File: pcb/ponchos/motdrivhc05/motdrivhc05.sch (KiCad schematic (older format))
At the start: 21 parts, among them J1 Screw_Terminal_1x06, J3 GW-040, J4 CONN_01X02, Q1 TIP31, U1 L293

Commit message: Agregado y modificado de nombres de nets en esquemático. Agregado de serigrafías con referencias en PCB.
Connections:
- net M1A: now also D1.2 (A), D5.1 (K), J1.4, U1.3 (1Y); no longer SH1.8, U1.2 (1A)
- net M2A: now also D3.2 (A), D7.1 (K), J1.6, U1.11 (3Y); no longer SH1.11 ((*/MOSI)_11), U1.7 (2A)
- net M2B: now reaches D4.2 (A), D8.1 (K), J1.5, U1.14 (4Y)
- net M1B: now reaches D2.2 (A), D6.1 (K), J1.3, U1.6 (2Y)
- net EXT: now reaches D9.1 (K), J4.2 (P2), Q1.2 (C)
- net M3A renamed 3A
- net M4A renamed 4A
- new net 1A: SH1.8, U1.2 (1A)
- new net 2A: SH1.11 ((*/MOSI)_11), U1.7 (2A)
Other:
- moved on the sheet: D9, J4
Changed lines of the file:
@@
 Connection ~ 6600 3675
 Wire Wire Line
-	7225 2375 10000 2375
-Wire Wire Line
-	7150 2575 9875 2575
-Wire Wire Line
-	7150 2775 9975 2775
-Wire Wire Line
-	7225 2975 9875 2975
+	7225 2375 9325 2375
+Wire Wire Line
+	7150 2575 9200 2575
+Wire Wire Line
+	7150 2775 9325 2775
+Wire Wire Line
+	7225 2975 9225 2975
 Wire Wire Line
 	7750 3350 7750 3450
@@
 	6400 1050 6400 1800
 Text Label 5775 2200 2    60   ~ 0
-M1A
+1A
 Wire Wire Line
 	6000 2200 5775 2200
 Text Label 5775 2400 2    60   ~ 0
-M2A
+2A
 Wire Wire Line
 	6000 2400 5775 2400
@@
 	6000 2800 5775 2800
 Text Label 5775 3000 2    60   ~ 0
-M3A
+3A
 Wire Wire Line
 	6000 3000 5775 3000
 Text Label 5775 3200 2    60   ~ 0
-M4A
+4A
 Wire Wire Line
 	6000 3200 5775 3200
 Text Label 3800 3450 0    60   ~ 0
-M1A
+1A
 Wire Wire Line
 	3575 3450 3800 3450
 Text Label 3800 3075 0    60   ~ 0
-M2A
+2A
 Wire Wire Line
 	3575 3075 3800 3075
@@
 	3575 3200 3800 3200
 Text Label 3800 2950 0    60   ~ 0
-M3A
+3A
 Wire Wire Line
 	3575 2950 3800 2950
 Text Label 3800 2825 0    60   ~ 0
-M4A
+4A
 Wire Wire Line
 	3575 2825 3800 2825
@@
 L CONN_01X02 J4
 U 1 1 59A1C921
-P 4900 5725
-F 0 "J4" H 4900 5875 50  0000 C CNN
-F 1 "CONN_01X02" V 5000 5725 50  0000 C CNN
-F 2 "Pin_Headers:Pin_Header_Straight_1x02" H 4900 5725 50  0001 C CNN
-F 3 "" H 4900 5725 50  0001 C CNN
-	1    4900 5725
-	1    0    0    -1
-$EndComp
-Wire Wire Line
-	4100 5775 4700 5775
+P 5175 5725
+F 0 "J4" H 5175 5875 50  0000 C CNN
+F 1 "CONN_01X02" V 5275 5725 50  0000 C CNN
+F 2 "Pin_Headers:Pin_Header_Straight_1x02" H 5175 5725 50  0001 C CNN
+F 3 "" H 5175 5725 50  0001 C CNN
+	1    5175 5725
+	1    0    0    -1
+$EndComp
+Wire Wire Line
+	4100 5775 4975 5775
 Wire Wire Line
 	4100 5775 4100 5975
@@
 L D_Schottky_Small D9
 U 1 1 59A1D6C4
-P 4600 6175
-F 0 "D9" V 4500 6000 50  0000 L CNN
-F 1 "1N5819" V 4625 5800 50  0000 L CNN
-F 2 "Diodes_ThroughHole:Diode_DO-41_SOD81_Horizontal_RM10" V 4600 6175 50  0001 C CNN
-F 3 "" V 4600 6175 50  0001 C CNN
-	1    4600 6175
-	0    -1   1    0
-$EndComp
-Wire Wire Line
-	4600 6075 4600 5775
-Connection ~ 4600 5775
-Wire Wire Line
-	4600 6275 4600 6450
-Wire Wire Line
-	4600 6450 4100 6450
+P 4450 6175
+F 0 "D9" V 4350 6000 50  0000 L CNN
+F 1 "1N5819" V 4475 5800 50  0000 L CNN
+F 2 "Diodes_ThroughHole:Diode_DO-41_SOD81_Horizontal_RM10" V 4450 6175 50  0001 C CNN
+F 3 "" V 4450 6175 50  0001 C CNN
+	1    4450 6175
+	0    -1   1    0
+$EndComp
+Wire Wire Line
+	4450 6075 4450 5775
+Connection ~ 4450 5775
+Wire Wire Line
+	4450 6275 4450 6450
+Wire Wire Line
+	4450 6450 4100 6450
 Connection ~ 4100 6450
 Text Label 3675 2450 0    60   ~ 0
@@
 Wire Wire Line
 	7150 3000 7000 3000
-NoConn ~ 4700 5675
+NoConn ~ 4975 5675
 $Comp
 L Screw_Terminal_1x06 J1
@@
 	10025 1975 10125 1975
 Wire Wire Line
-	10000 2375 10000 2575
-Wire Wire Line
-	10000 2575 10125 2575
-Wire Wire Line
-	9875 2575 9875 2475
-Wire Wire Line
-	9875 2475 10050 2475
-Wire Wire Line
-	10050 2475 10050 2375
-Wire Wire Line
-	10050 2375 10125 2375
-Wire Wire Line
-	9975 2775 9975 2975
-Wire Wire Line
-	9975 2975 10125 2975
-Wire Wire Line
-	9875 2975 9875 2850
-Wire Wire Line
-	9875 2850 10075 2850
-Wire Wire Line
-	10075 2850 10075 2775
-Wire Wire Line
-	10075 2775 10125 2775
+	9325 2375 9325 2575
+Wire Wire Line
+	9325 2575 10125 2575
+Wire Wire Line
+	9200 2575 9200 2475
+Wire Wire Line
+	9200 2475 9375 2475
+Wire Wire Line
+	9375 2475 9375 2375
+Wire Wire Line
+	9375 2375 10125 2375
+Wire Wire Line
+	9325 2775 9325 2975
+Wire Wire Line
+	9325 2975 10125 2975
+Wire Wire Line
+	9225 2975 9225 2850
+Wire Wire Line
+	9225 2850 9425 2850
+Wire Wire Line
+	9425 2850 9425 2775
+Wire Wire Line
+	9425 2775 10125 2775
+Text Label 9650 2575 0    60   ~ 0
+M1A
+Text Label 9650 2375 0    60   ~ 0
+M1B
+Text Label 9650 2975 0    60   ~ 0
+M2A
+Text Label 9650 2775 0    60   ~ 0
+M2B
+Text Label 4625 5775 0    60   ~ 0
+EXT
 $EndSCHEMATC

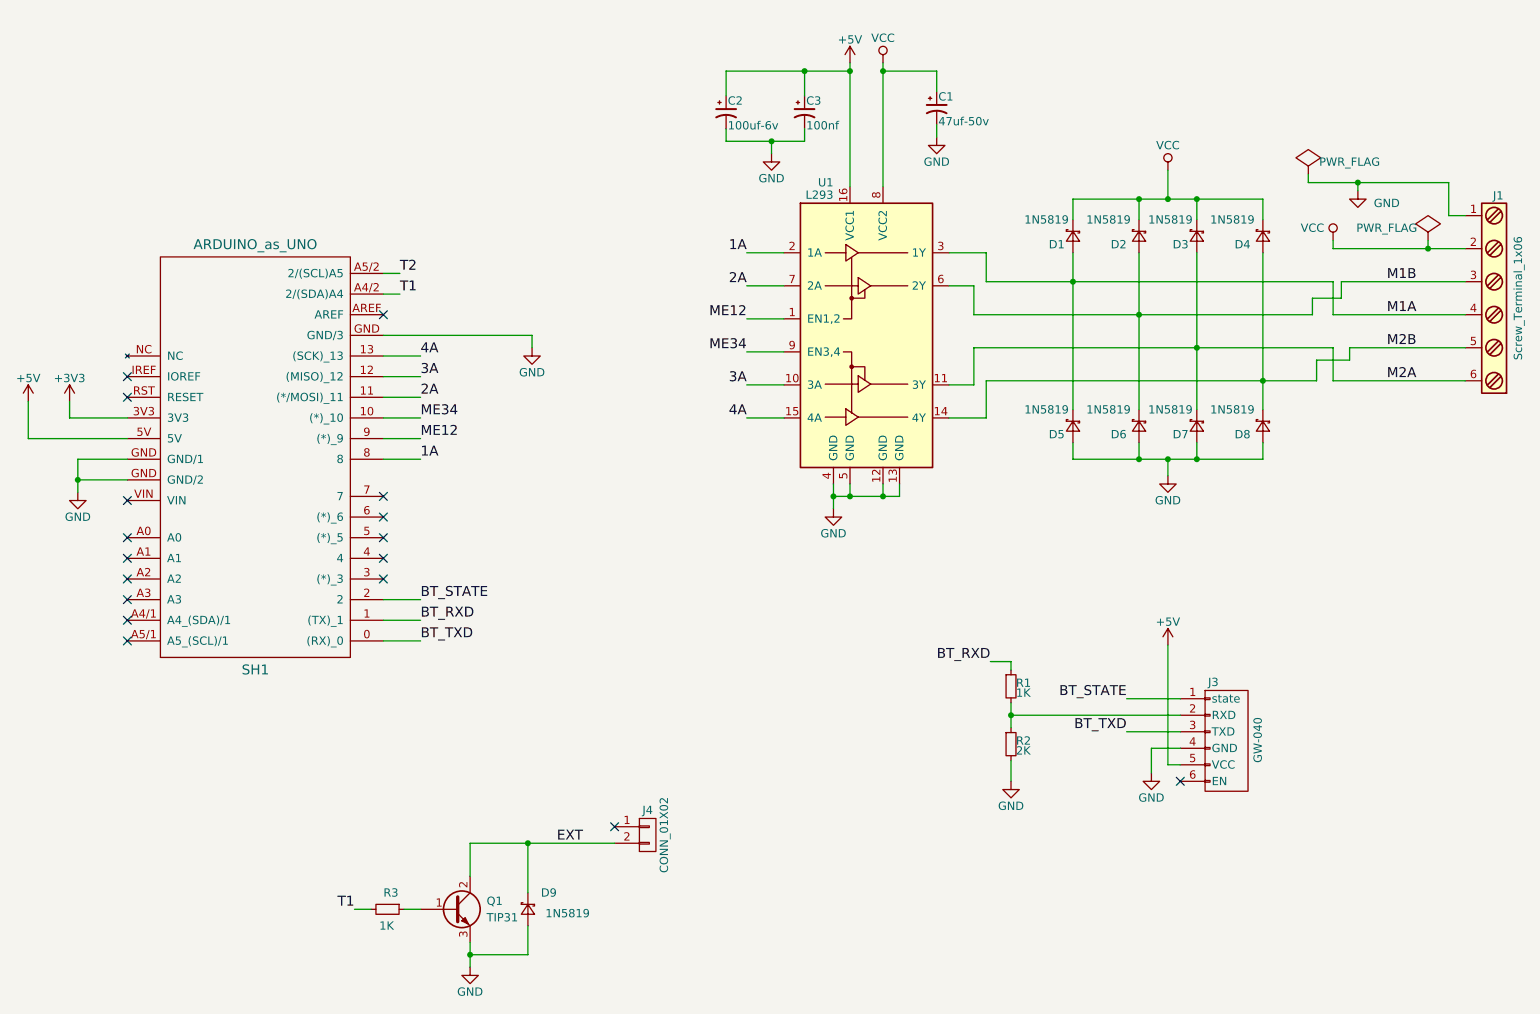
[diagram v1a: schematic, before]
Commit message: Corrimiento del conector, agujeros para disipador, giro capacitores para poner acostados, cambio pin del key/status, se quitó el transistor para rele.
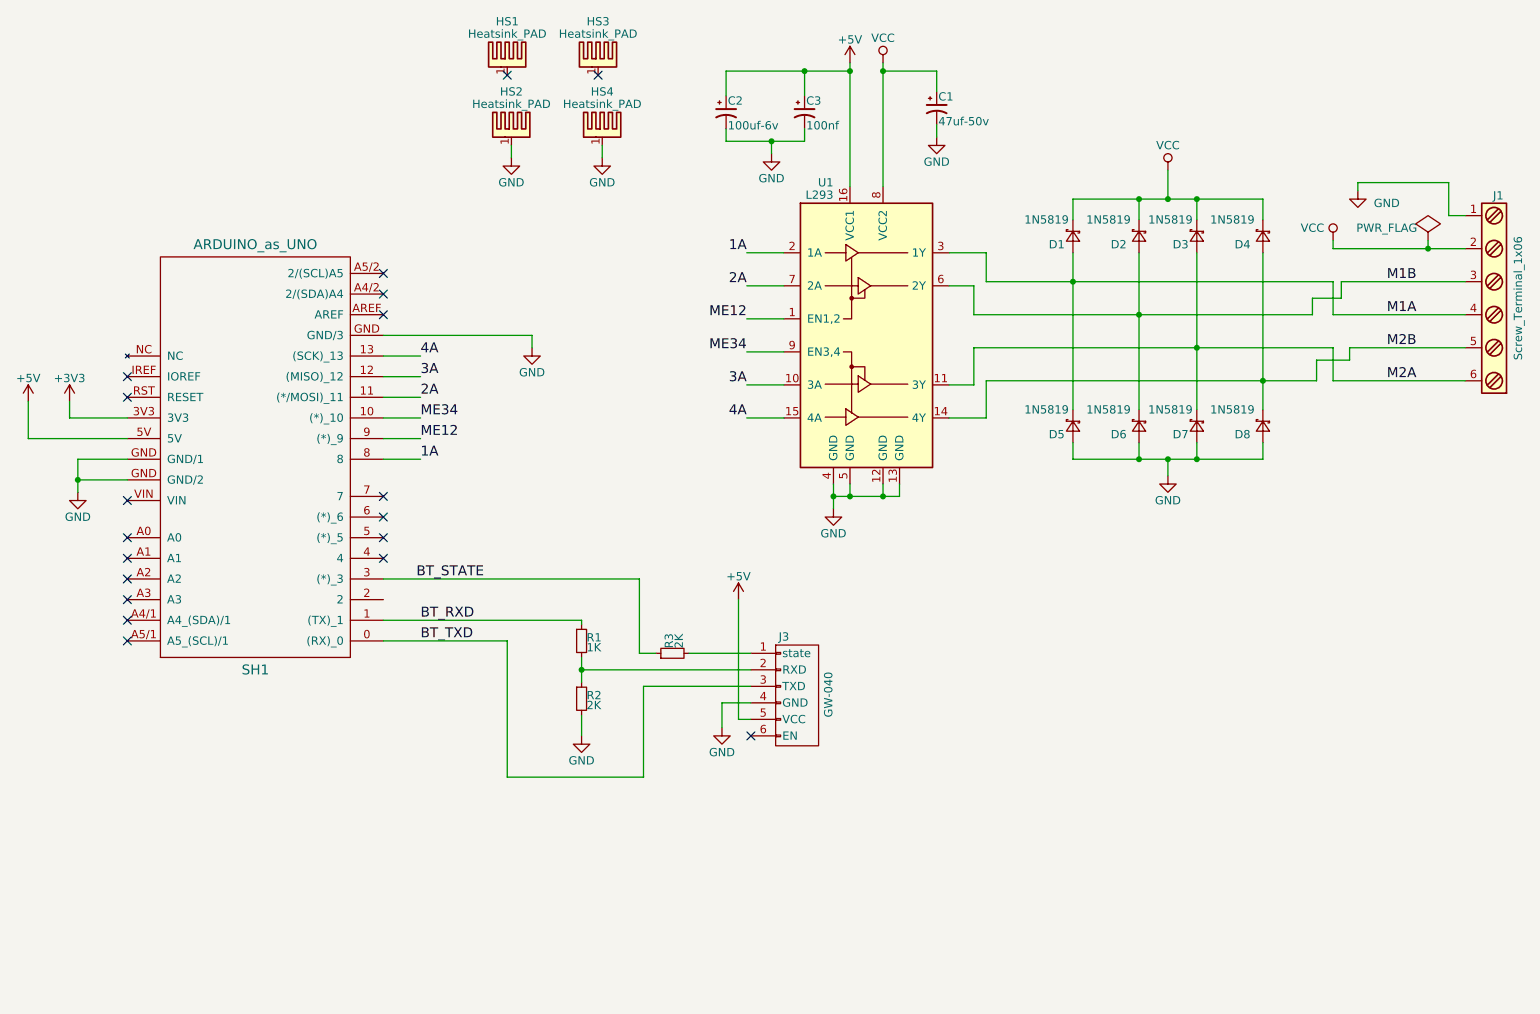
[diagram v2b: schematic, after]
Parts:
- removed D9: 1N5819, Diodes_ThroughHole:Diode_DO-41_SOD81_Horizontal_RM10, symbol D_Schottky_Small
- removed J4: CONN_01X02, Pin_Headers:Pin_Header_Straight_1x02, symbol CONN_01X02
- removed Q1: TIP31, TO_SOT_Packages_THT:TO-220_Neutral123_Horizontal_LargePads, symbol Q_NPN_BCE
- added HS1, HS2, HS3, HS4: Heatsink_PAD, Mounting_Holes:MountingHole_3.2mm_M3_ISO14580, symbol Heatsink_PAD
- R3: value 1K -> 2K
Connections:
- net BT_STATE: now also R3.1, SH1.3 ((*)_3); no longer J3.1 (state), SH1.2
- net GND: now also HS2.1, HS4.1
- net T1: no longer names the net of SH1.A4/2 (2/(SDA)A4)
- net T1: no longer R3.2
- net T2: no longer names the net of SH1.A5/2 (2/(SCL)A5)
- new net: J3.1 (state), R3.2
- no-connect marks 17 -> 19
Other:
- moved on the sheet: J3, R1, R2
